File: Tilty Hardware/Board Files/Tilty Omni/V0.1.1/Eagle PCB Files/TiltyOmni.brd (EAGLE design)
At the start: 41.9 x 52.1 mm, 37 parts, among them U1 TEENSY_3.0_ALLPINSTEENSY_3.0_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, U2 HC-09_BREAKOUT, U4 LM2931, U5 MPU-6050, U7 SPI_FLASH-X25XXSMD

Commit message: Lots of little changes
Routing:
- net A12: track 44.3 -> 44.8 mm
- net +3V3: track 151.7 -> 151.2 mm
- net MEMORY_CS: track 35.2 -> 34.7 mm
- net 26: track 35.3 -> 34.8 mm
- net IMU_INT: track 4.32 -> 3.81 mm
- net BT_CMD: track 37.7 -> 37.2 mm
- net 32: track 37.1 -> 37.6 mm
- net 25: track 34.3 -> 33.8 mm
- net 24: track 34.6 -> 34.1 mm
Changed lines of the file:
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@@
 <wire x1="15.748" y1="27.178" x2="15.748" y2="32.512" width="0.2032" layer="1"/>
 <wire x1="15.748" y1="32.512" x2="16.256" y2="33.02" width="0.2032" layer="1"/>
-<wire x1="16.256" y1="33.02" x2="19.685" y2="33.02" width="0.2032" layer="1"/>
+<wire x1="16.256" y1="33.02" x2="19.177" y2="33.02" width="0.2032" layer="1"/>
 <via x="29.972" y="25.4" extent="1-16" drill="0.3302"/>
-<via x="19.685" y="33.02" extent="1-16" drill="0.3302"/>
-<wire x1="19.685" y1="33.02" x2="26.162" y2="33.02" width="0.2032" layer="16"/>
+<via x="19.177" y="33.02" extent="1-16" drill="0.3302"/>
+<wire x1="19.177" y1="33.02" x2="26.162" y2="33.02" width="0.2032" layer="16"/>
 <wire x1="26.2255" y1="27.0505" x2="26.205" y2="27.03" width="0.2032" layer="16"/>
 <wire x1="27.455" y1="25.28" x2="26.663" y2="25.28" width="0.2032" layer="16"/>
@@
 <wire x1="25.908" y1="28.448" x2="20.193" y2="28.448" width="0.2032" layer="16"/>
 <wire x1="20.193" y1="28.448" x2="19.685" y2="28.956" width="0.2032" layer="16"/>
-<wire x1="19.685" y1="28.956" x2="19.685" y2="33.02" width="0.2032" layer="16"/>
+<wire x1="19.685" y1="28.956" x2="19.177" y2="33.02" width="0.2032" layer="16"/>
 </signal>
 <signal name="AGND">
-<contactref element="U1" pad="AGND"/>
 <contactref element="JP7" pad="19"/>
 <wire x1="28.575" y1="48.26" x2="28.702" y2="48.26" width="0.2032" layer="1"/>
@@
 <wire x1="36.5125" y1="46.1645" x2="39.116" y2="46.1645" width="0.2032" layer="1"/>
 <wire x1="39.116" y1="46.1645" x2="40.5765" y2="47.625" width="0.2032" layer="1"/>
+<contactref element="U1" pad="AGND"/>
 </signal>
 <signal name="VBAT">
@@
 <contactref element="U1" pad="28"/>
 <contactref element="JP6" pad="1"/>
-<wire x1="19.685" y1="20.32" x2="15.748" y2="20.32" width="0.1524" layer="1"/>
+<wire x1="19.177" y1="20.32" x2="15.748" y2="20.32" width="0.1524" layer="1"/>
 <wire x1="15.748" y1="20.32" x2="15.494" y2="20.066" width="0.1524" layer="1"/>
 <wire x1="15.494" y1="20.066" x2="15.494" y2="19.05" width="0.1524" layer="1"/>
@@
 <wire x1="15.24" y1="36.83" x2="24.384" y2="36.83" width="0.1524" layer="1"/>
 <wire x1="24.384" y1="36.83" x2="24.765" y2="36.449" width="0.1524" layer="1"/>
-<wire x1="24.765" y1="36.449" x2="24.765" y2="35.56" width="0.1524" layer="1"/>
+<wire x1="24.765" y1="36.449" x2="25.273" y2="35.56" width="0.1524" layer="1"/>
 <wire x1="21.8685" y1="14.0335" x2="21.844" y2="14.058" width="0.1524" layer="1"/>
 <wire x1="21.59" y1="15.113" x2="21.59" y2="14.312" width="0.1524" layer="1"/>
@@
 <contactref element="U7" pad="1"/>
 <contactref element="U1" pad="27"/>
-<via x="19.685" y="22.86" extent="1-16" drill="0.3302"/>
-<wire x1="19.685" y1="22.86" x2="17.526" y2="22.86" width="0.2032" layer="16"/>
+<via x="19.177" y="22.86" extent="1-16" drill="0.3302"/>
+<wire x1="19.177" y1="22.86" x2="17.526" y2="22.86" width="0.2032" layer="16"/>
 <wire x1="17.526" y1="22.86" x2="17.145" y2="22.479" width="0.2032" layer="16"/>
 <via x="17.145" y="11.049" extent="1-16" drill="0.3302"/>
@@
 <contactref element="MPU_INT" pad="1"/>
 <via x="27.2415" y="30.48" extent="1-16" drill="0.3302"/>
-<wire x1="27.2415" y1="30.48" x2="24.765" y2="30.48" width="0.1524" layer="1"/>
+<wire x1="27.2415" y1="30.48" x2="25.273" y2="30.48" width="0.1524" layer="1"/>
 <wire x1="25.4" y1="30.48" x2="27.2415" y2="30.48" width="0.1524" layer="16"/>
 </signal>
@@
 <wire x1="32.258" y1="20.32" x2="32.258" y2="22.118" width="0.1524" layer="1"/>
 <wire x1="32.258" y1="22.118" x2="32.27" y2="22.13" width="0.1524" layer="1"/>
-<wire x1="24.765" y1="33.02" x2="26.924" y2="33.02" width="0.254" layer="1"/>
+<wire x1="25.273" y1="33.02" x2="26.924" y2="33.02" width="0.254" layer="1"/>
 <wire x1="26.924" y1="33.02" x2="27.432" y2="33.528" width="0.254" layer="1"/>
 <wire x1="27.432" y1="33.528" x2="27.432" y2="33.782" width="0.254" layer="1"/>
@@
 <contactref element="U1" pad="24"/>
 <contactref element="JP6" pad="5"/>
-<wire x1="19.685" y1="30.48" x2="16.51" y2="30.48" width="0.1524" layer="1"/>
+<wire x1="19.177" y1="30.48" x2="16.51" y2="30.48" width="0.1524" layer="1"/>
 <wire x1="16.51" y1="30.48" x2="16.256" y2="30.226" width="0.1524" layer="1"/>
 <wire x1="16.256" y1="30.226" x2="16.256" y2="22.225" width="0.1524" layer="1"/>
@@
 <contactref element="U1" pad="25"/>
 <contactref element="JP6" pad="4"/>
-<wire x1="19.685" y1="27.94" x2="17.018" y2="27.94" width="0.1524" layer="1"/>
+<wire x1="19.177" y1="27.94" x2="17.018" y2="27.94" width="0.1524" layer="1"/>
 <wire x1="17.018" y1="27.94" x2="16.764" y2="27.686" width="0.1524" layer="1"/>
 <wire x1="16.764" y1="27.686" x2="16.764" y2="21.717" width="0.1524" layer="1"/>
@@
 <contactref element="U1" pad="26"/>
 <contactref element="JP6" pad="3"/>
-<wire x1="19.685" y1="25.4" x2="17.526" y2="25.4" width="0.1524" layer="1"/>
+<wire x1="19.177" y1="25.4" x2="17.526" y2="25.4" width="0.1524" layer="1"/>
 <wire x1="17.526" y1="25.4" x2="17.272" y2="25.146" width="0.1524" layer="1"/>
 <wire x1="17.272" y1="25.146" x2="17.272" y2="21.082" width="0.1524" layer="1"/>
@@
 <contactref element="U1" pad="29"/>
 <contactref element="JP7" pad="1"/>
-<via x="24.765" y="20.32" extent="1-16" drill="0.3302"/>
+<via x="25.273" y="20.32" extent="1-16" drill="0.3302"/>
 <wire x1="39.37" y1="3.1115" x2="40.5765" y2="1.905" width="0.1524" layer="16"/>
 <wire x1="31.877" y1="5.715" x2="31.242" y2="6.35" width="0.1524" layer="16"/>
@@
 <wire x1="25.654" y1="6.604" x2="24.13" y2="6.604" width="0.1524" layer="16"/>
 <wire x1="24.13" y1="9.144" x2="24.765" y2="9.779" width="0.1524" layer="16"/>
-<wire x1="24.765" y1="9.779" x2="24.765" y2="20.32" width="0.1524" layer="16"/>
+<wire x1="24.765" y1="9.779" x2="25.273" y2="20.32" width="0.1524" layer="16"/>
 <wire x1="24.13" y1="9.144" x2="24.13" y2="6.604" width="0.1524" layer="1"/>
 </signal>
@@
 <contactref element="U1" pad="30"/>
 <contactref element="JP7" pad="2"/>
-<via x="24.765" y="22.86" extent="1-16" drill="0.3302"/>
-<wire x1="24.765" y1="22.86" x2="25.4" y2="22.225" width="0.1524" layer="16"/>
+<via x="25.273" y="22.86" extent="1-16" drill="0.3302"/>
+<wire x1="25.273" y1="22.86" x2="25.4" y2="22.225" width="0.1524" layer="16"/>
 <wire x1="25.4" y1="22.225" x2="25.4" y2="7.874" width="0.1524" layer="16"/>
 <via x="25.4" y="7.874" extent="1-16" drill="0.3302"/>
@@
 <contactref element="U1" pad="31"/>
 <contactref element="JP7" pad="3"/>
-<via x="24.765" y="25.4" extent="1-16" drill="0.3302"/>
+<via x="25.273" y="25.4" extent="1-16" drill="0.3302"/>
 <via x="22.225" y="24.13" extent="1-16" drill="0.3302"/>
 <via x="29.845" y="18.288" extent="1-16" drill="0.3302"/>
@@
 <wire x1="31.496" y1="7.62" x2="32.131" y2="6.985" width="0.1524" layer="16"/>
 <wire x1="32.131" y1="6.985" x2="40.5765" y2="6.985" width="0.1524" layer="16"/>
-<wire x1="24.765" y1="25.4" x2="24.765" y2="24.511" width="0.1524" layer="16"/>
+<wire x1="25.273" y1="25.4" x2="24.765" y2="24.511" width="0.1524" layer="16"/>
 <wire x1="24.765" y1="24.511" x2="24.384" y2="24.13" width="0.1524" layer="16"/>
 <wire x1="24.384" y1="24.13" x2="22.225" y2="24.13" width="0.1524" layer="16"/>
@@
 <contactref element="JP7" pad="4"/>
 <via x="29.845" y="19.2405" extent="1-16" drill="0.3302"/>
-<wire x1="24.765" y1="27.94" x2="23.622" y2="27.94" width="0.1524" layer="1"/>
+<wire x1="25.273" y1="27.94" x2="23.622" y2="27.94" width="0.1524" layer="1"/>
 <wire x1="23.622" y1="27.94" x2="22.733" y2="27.051" width="0.1524" layer="1"/>
 <wire x1="22.733" y1="19.4945" x2="22.987" y2="19.2405" width="0.1524" layer="1"/>
@@
 <contactref element="U1" pad="A12"/>
 <contactref element="JP7" pad="5"/>
-<via x="19.685" y="35.56" extent="1-16" drill="0.3302"/>
-<wire x1="19.685" y1="35.56" x2="26.924" y2="35.56" width="0.1524" layer="16"/>
+<via x="19.177" y="35.56" extent="1-16" drill="0.3302"/>
+<wire x1="19.177" y1="35.56" x2="26.924" y2="35.56" width="0.1524" layer="16"/>
 <wire x1="26.924" y1="35.56" x2="27.178" y2="35.814" width="0.1524" layer="16"/>
 <wire x1="27.178" y1="35.814" x2="27.178" y2="36.195" width="0.1524" layer="16"/>

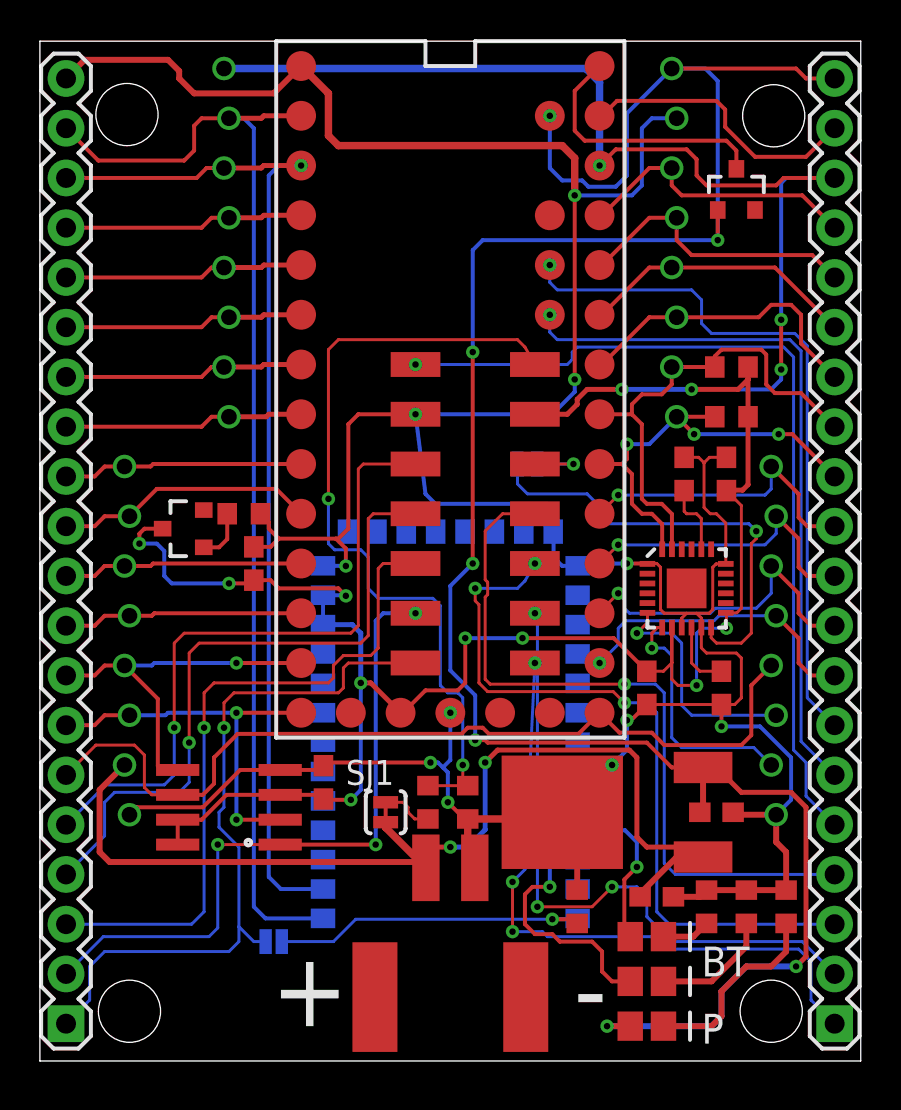
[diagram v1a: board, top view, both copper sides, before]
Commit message: Updated Tilty Omni to remove possible short circuits between PCB and Teensy
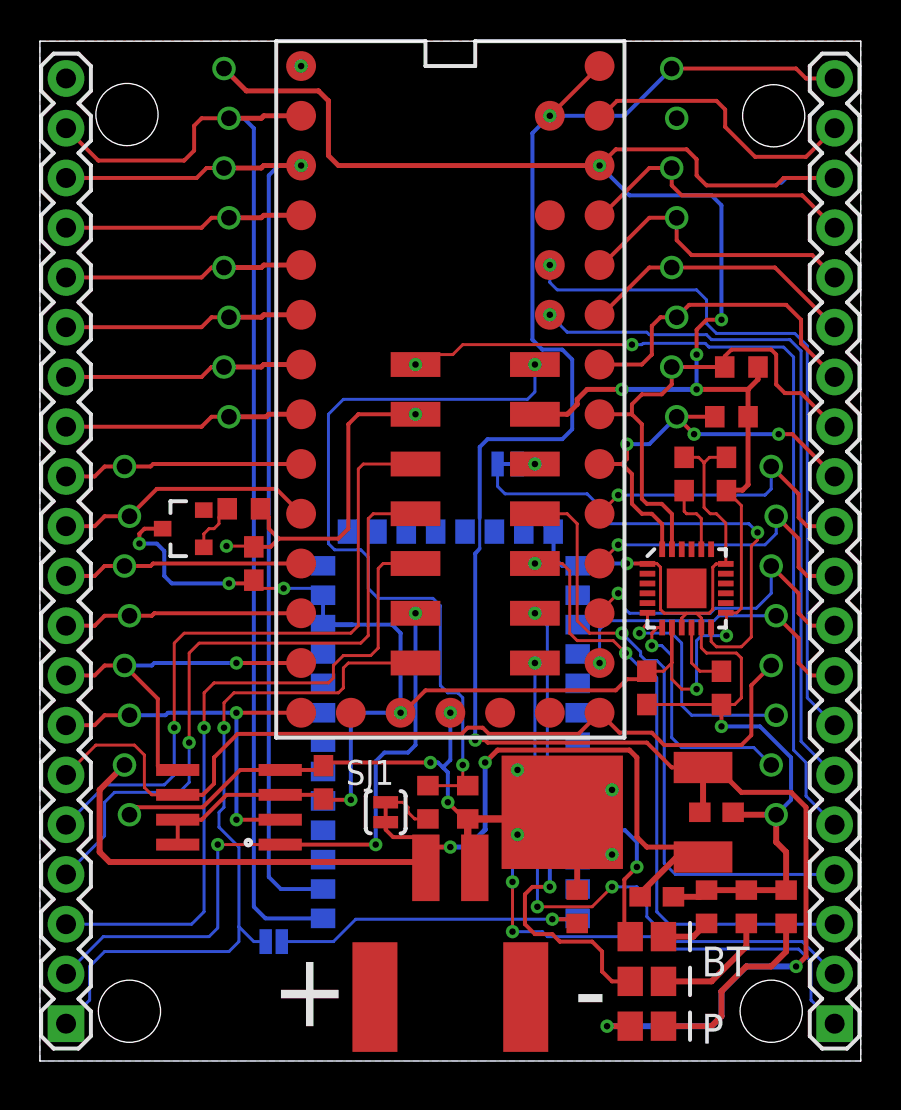
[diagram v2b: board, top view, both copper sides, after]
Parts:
- removed D4: (no value), SparkFun-DiscreteSemi:SOT23-3
- moved MPU_INT 1.02 mm to (23.9, 30.5)
- moved R1 0.51 mm to (35.8, 35.4)
- moved R9 0.25 mm to (10.4, 28.2)
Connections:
- removed net N$4: D4.3, U1.VIN
- net +5V: now also U1.VIN; no longer D4.1
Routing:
- net GND: track 190.6 -> 110.2 mm, vias 11 -> 12
- net +5V: track 115.0 -> 99.1 mm, vias 7 -> 4
- net N$4: track 13.4 -> 0.00 mm
- net 31: track 37.8 -> 31.8 mm, vias 3 -> 2
- net 32: track 37.6 -> 31.8 mm
- net IMU_INT: track 3.81 -> 0.89 mm
- net BATT_SENSE: track 41.4 -> 39.1 mm
- net N$16: track 22.7 -> 24.2 mm
- net +3V3: track 151.2 -> 149.7 mm, vias 14 -> 12
- net 20/A6: track 15.6 -> 16.4 mm
- net 14/A0: track 15.5 -> 16.0 mm
- net A11: track 36.5 -> 36.0 mm
- net A12: vias 1 -> 2
- added copper zone on layer 16, net GND

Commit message: Added vias to as many SMT Teensy pads as possible to ease reflow soldering
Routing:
- net SERVO_4: vias 0 -> 1
- net SERVO_3: vias 0 -> 1
- net SERVO_2: vias 0 -> 1
- net SERVO_1: vias 0 -> 1
- net BLUETOOTH_RX: vias 0 -> 1
- net 8/TX3: vias 0 -> 1
- net 7/RX3: vias 0 -> 1
- net 6/PWM: vias 0 -> 1
- net 5/PWM: vias 0 -> 1
- net 4/PWM: vias 0 -> 1
- net 3V_SDA: vias 3 -> 4
- net 3V_SCL: vias 0 -> 1
- net 26: vias 1 -> 2
- net 24: vias 1 -> 2
- net 21/A7: vias 0 -> 1
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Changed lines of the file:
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@@
 <signal name="AREF">
 <contactref element="U1" pad="AREF"/>
+<via x="26.035" y="43.18" extent="1-16" drill="0.3302"/>
 </signal>
 <signal name="N$1">
@@
 <wire x1="3.302" y1="27.813" x2="2.794" y2="27.305" width="0.2032" layer="1"/>
 <wire x1="2.794" y1="27.305" x2="1.3335" y2="27.305" width="0.2032" layer="1"/>
+<via x="13.335" y="27.94" extent="1-16" drill="0.3302"/>
 </signal>
 <signal name="7/RX3">
@@
 <wire x1="3.302" y1="30.353" x2="2.794" y2="29.845" width="0.2032" layer="1"/>
 <wire x1="2.794" y1="29.845" x2="1.3335" y2="29.845" width="0.2032" layer="1"/>
+<via x="13.335" y="30.48" extent="1-16" drill="0.3302"/>
 </signal>
 <signal name="MEMORY_CS">
@@
 <wire x1="8.763" y1="37.973" x2="8.255" y2="37.465" width="0.2032" layer="1"/>
 <wire x1="8.255" y1="37.465" x2="1.3335" y2="37.465" width="0.2032" layer="1"/>
+<via x="13.335" y="38.1" extent="1-16" drill="0.3302"/>
 </signal>
 <signal name="SERVO_2">
@@
 <wire x1="8.763" y1="40.513" x2="8.255" y2="40.005" width="0.2032" layer="1"/>
 <wire x1="8.255" y1="40.005" x2="1.3335" y2="40.005" width="0.2032" layer="1"/>
+<via x="13.335" y="40.64" extent="1-16" drill="0.3302"/>
 </signal>
 <signal name="SERVO_1">
@@
 <wire x1="8.763" y1="43.053" x2="8.255" y2="42.545" width="0.2032" layer="1"/>
 <wire x1="8.255" y1="42.545" x2="1.3335" y2="42.545" width="0.2032" layer="1"/>
+<via x="13.335" y="43.18" extent="1-16" drill="0.3302"/>
 </signal>
 <signal name="BLUETOOTH_TX">
@@
 <wire x1="7.366" y1="45.974" x2="2.9845" y2="45.974" width="0.2032" layer="1"/>
 <wire x1="2.9845" y1="45.974" x2="1.3335" y2="47.625" width="0.2032" layer="1"/>
+<via x="13.335" y="48.26" extent="1-16" drill="0.3302"/>
 </signal>
 <signal name="5V_SDA">
@@
 <wire x1="28.702" y1="43.18" x2="31.115" y2="45.593" width="0.2032" layer="1"/>
 <wire x1="31.115" y1="45.593" x2="32.258" y2="45.593" width="0.2032" layer="1"/>
+<via x="28.575" y="43.18" extent="1-16" drill="0.3302"/>
 </signal>
 <signal name="SERVO_3">
@@
 <wire x1="33.274" y1="41.148" x2="39.4335" y2="41.148" width="0.2032" layer="1"/>
 <wire x1="39.4335" y1="41.148" x2="40.5765" y2="40.005" width="0.2032" layer="1"/>
+<via x="28.575" y="40.64" extent="1-16" drill="0.3302"/>
 </signal>
 <signal name="21/A7">
@@
 <wire x1="32.258" y1="40.513" x2="37.5285" y2="40.513" width="0.2032" layer="1"/>
 <wire x1="37.5285" y1="40.513" x2="40.5765" y2="37.465" width="0.2032" layer="1"/>
+<via x="28.575" y="38.1" extent="1-16" drill="0.3302"/>
 </signal>
 <signal name="20/A6">
@@
 <wire x1="38.1" y1="38.608" x2="33.147" y2="38.608" width="0.2032" layer="1"/>
 <wire x1="33.147" y1="38.608" x2="32.512" y2="37.973" width="0.2032" layer="1"/>
+<via x="28.575" y="35.56" extent="1-16" drill="0.3302"/>
 </signal>
 <signal name="3V_SCL">
@@
 <wire x1="37.592" y1="34.544" x2="38.0365" y2="34.0995" width="0.2032" layer="1"/>
 <wire x1="38.0365" y1="34.0995" x2="38.862" y2="34.0995" width="0.2032" layer="1"/>
+<via x="28.575" y="33.02" extent="1-16" drill="0.3302"/>
 </signal>
 <signal name="3V_SDA">
@@
 <wire x1="29.972" y1="31.496" x2="31.115" y2="31.496" width="0.2032" layer="16"/>
 <wire x1="31.115" y1="31.496" x2="32.512" y2="32.893" width="0.2032" layer="16"/>
+<via x="28.575" y="30.48" extent="1-16" drill="0.3302"/>
 </signal>
 <signal name="+3V3">
@@
 <contactref element="U1" pad="VIN"/>
 <wire x1="28.575" y1="50.8" x2="26.035" y2="48.26" width="0.2032" layer="1"/>
+<via x="28.575" y="50.8" extent="1-16" drill="0.3302"/>
 </signal>
 <signal name="VCC">
@@
 <wire x1="6.858" y1="14.605" x2="6.35" y2="14.097" width="0.1524" layer="16"/>
 <wire x1="6.35" y1="14.097" x2="3.3655" y2="14.097" width="0.1524" layer="16"/>
+<via x="19.177" y="30.48" extent="1-16" drill="0.3302"/>
 </signal>
 <signal name="25">
@@
 <wire x1="8.382" y1="7.62" x2="7.747" y2="6.985" width="0.1524" layer="16"/>
 <wire x1="7.747" y1="6.985" x2="1.3335" y2="6.985" width="0.1524" layer="16"/>
+<via x="19.177" y="25.4" extent="1-16" drill="0.3302"/>
 </signal>
 <signal name="29">
@@
 <wire x1="8.763" y1="35.433" x2="8.255" y2="34.925" width="0.2032" layer="1"/>
 <wire x1="8.255" y1="34.925" x2="1.3335" y2="34.925" width="0.2032" layer="1"/>
+<via x="13.335" y="35.56" extent="1-16" drill="0.3302"/>
 </signal>
 <signal name="6/PWM">
@@
 <wire x1="8.763" y1="32.893" x2="8.255" y2="32.385" width="0.2032" layer="1"/>
 <wire x1="8.255" y1="32.385" x2="1.3335" y2="32.385" width="0.2032" layer="1"/>
+<via x="13.335" y="33.02" extent="1-16" drill="0.3302"/>
 </signal>
 <signal name="N$5">
@@
 <wire x1="9.144" y1="27.774" x2="9.564" y2="28.194" width="0.1524" layer="1"/>
 </signal>
+<signal name="N$4">
+<via x="23.495" y="17.78" extent="1-16" drill="0.3302"/>
+</signal>
 </signals>
